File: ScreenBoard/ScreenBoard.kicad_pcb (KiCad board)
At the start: 4 copper layers, 37.5 x 35.6 mm, 21 parts, among them J3 Conn_01x09_Male, K1 K_0051, U1 U_0076

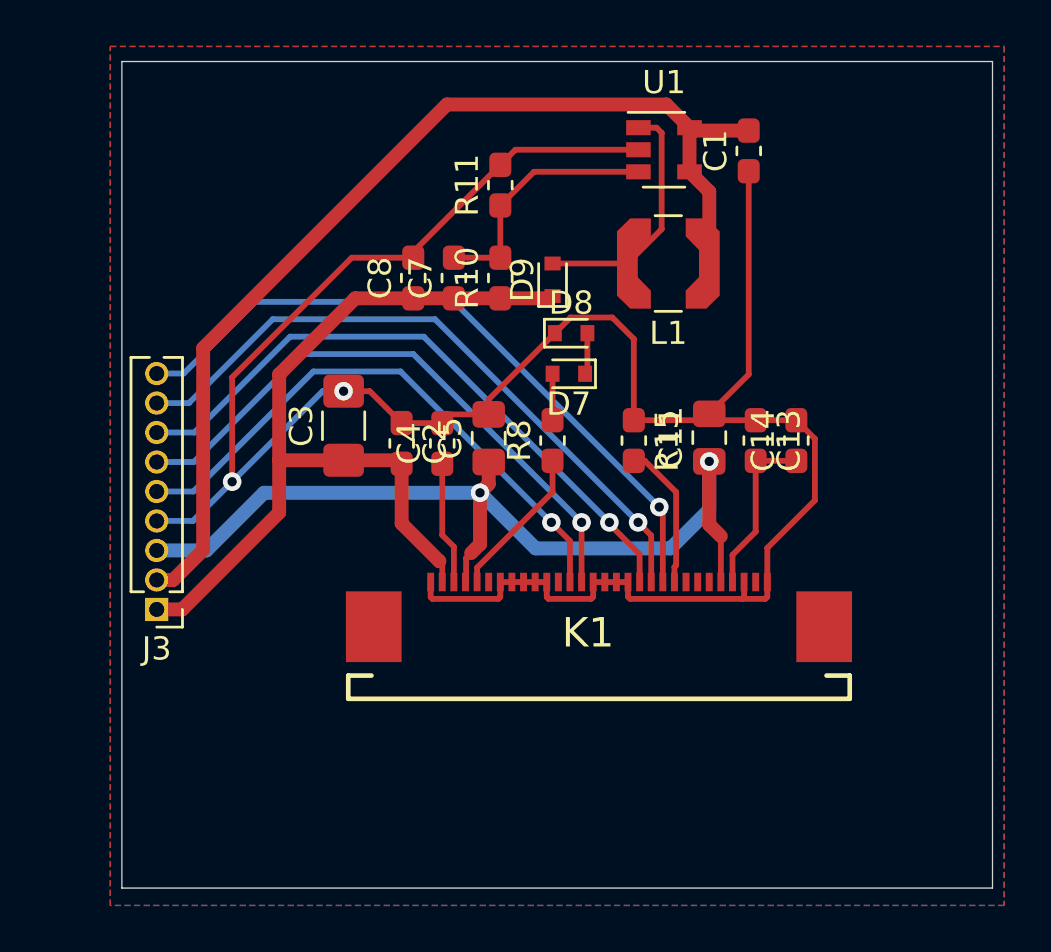
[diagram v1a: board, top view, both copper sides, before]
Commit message: fix: add missing rules and components
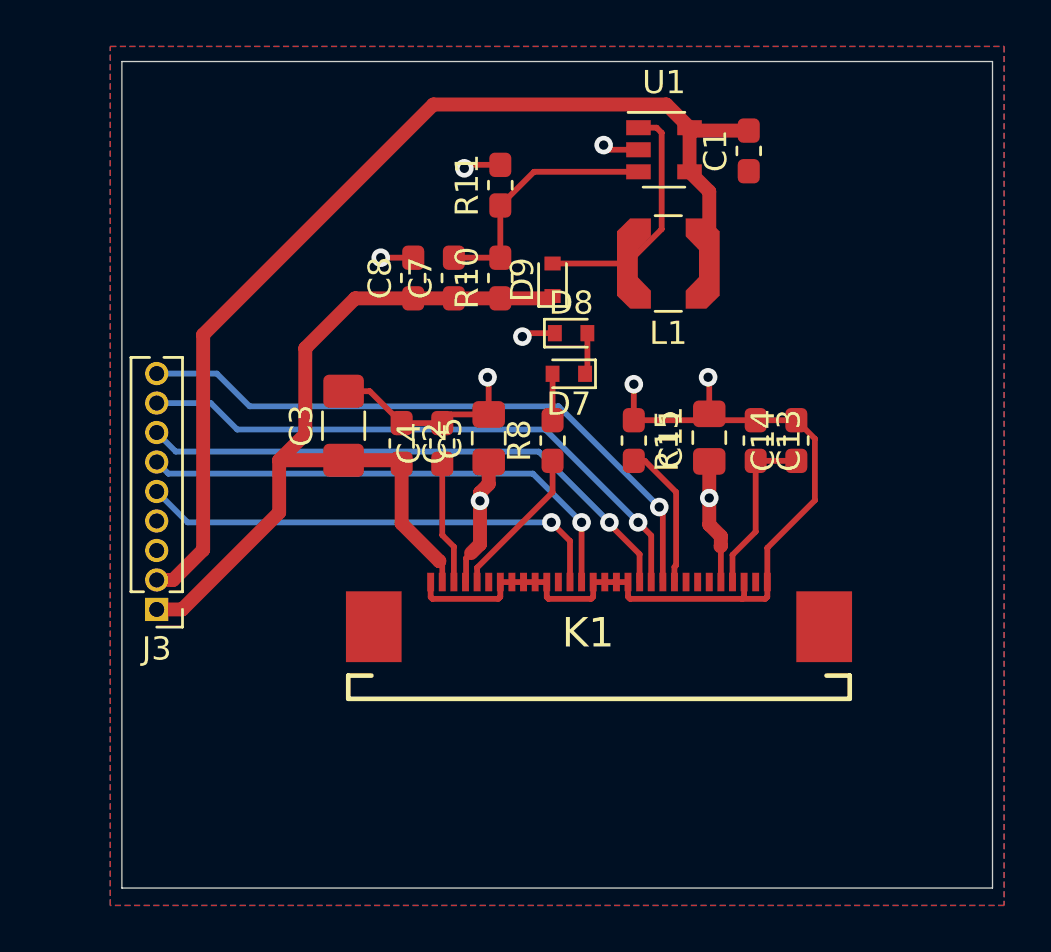
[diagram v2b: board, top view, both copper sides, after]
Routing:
- net GND: track 101.6 -> 52.5 mm, vias 2 -> 7
- net +3V3: track 39.6 -> 11.4 mm
- net /SPI1_MOSI: track 24.7 -> 20.5 mm
- net /SPI1_SCK: track 25.8 -> 21.9 mm
- net /OLED_CS: track 27.6 -> 24.2 mm
- net /OLED_DC: track 28.7 -> 25.7 mm
- net /OLED_RST: track 29.9 -> 27.3 mm

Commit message: fix: change screen connector footprint and adjust its mechanical position
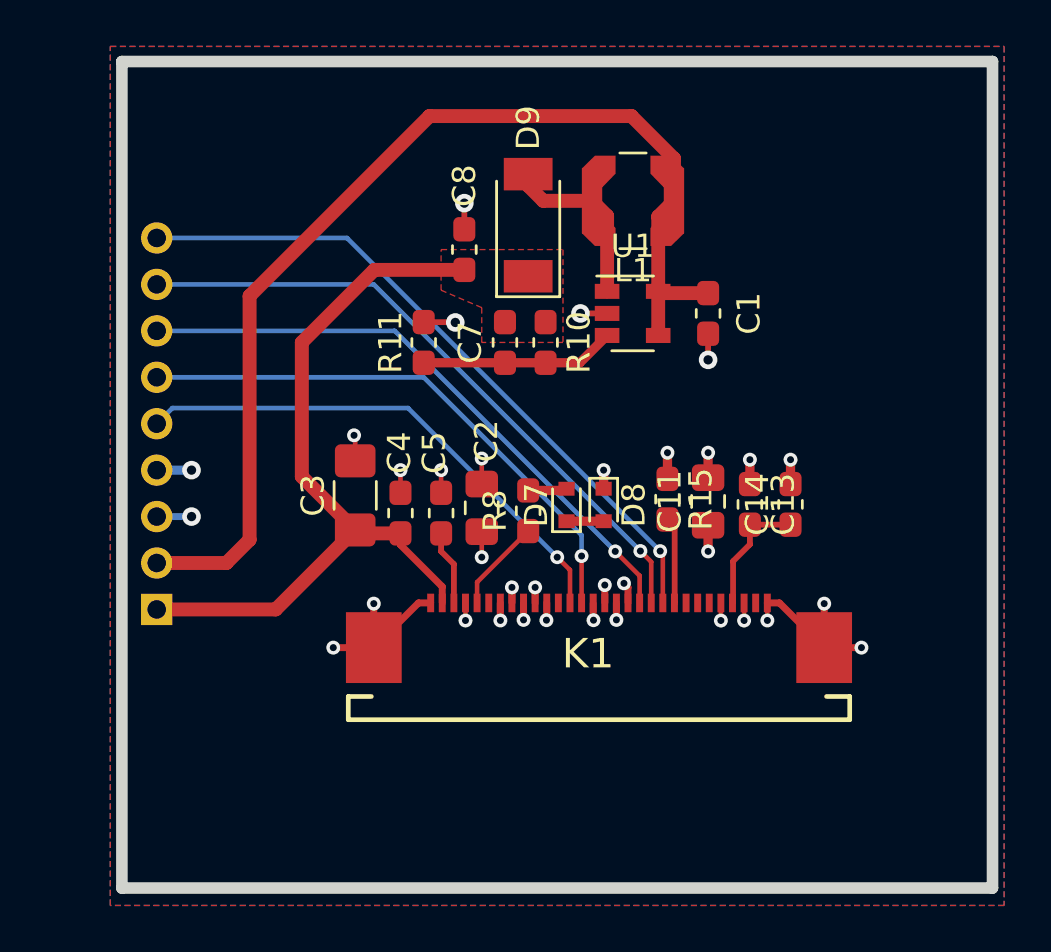
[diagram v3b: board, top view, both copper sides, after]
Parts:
- D9: footprint Diode_SMD:D_SOD-523 -> Diode_SMD:D_SOD-128
- J3: footprint Connector_PinHeader_1.27mm:PinHeader_1x09_P1.27mm_Vertical -> Connector_PinHeader_2.00mm:PinHeader_1x09_P2.00mm_Vertical; moved to B.Cu
- moved R11 7.54 mm to (114.0, 60.5)
- moved D8 7.53 mm to (121.8, 67.5), turned to 270 degrees
- moved C1 7.22 mm to (126.2, 59.2)
- moved U1 7.18 mm to (123.0, 59.2)
- moved D7 5.65 mm to (120.2, 67.5), turned to 90 degrees
- moved C7 3.54 mm to (117.5, 60.5), turned to 270 degrees
- moved R10 3.39 mm to (119.2, 60.5), turned to 270 degrees
- moved R8 3.20 mm to (118.5, 67.8)
- moved L1 3.10 mm to (123.0, 54.4)
- moved C3 3.04 mm to (111.0, 67.1)
- moved C5 3.01 mm to (116.5, 67.6)
- moved C2 3.00 mm to (113.0, 67.8)
- moved C4 3.00 mm to (114.8, 67.8)
- moved R15 2.91 mm to (124.5, 67.2)
- moved C13 2.76 mm to (128.1, 67.5)
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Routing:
- net GND: track 52.5 -> 38.9 mm, vias 7 -> 29
- net +12V: track 39.6 -> 33.0 mm
- net +3V3: track 11.4 -> 5.24 mm, vias 2 -> 5
- net Net-(D9-Pad2): track 10.6 -> 7.69 mm
- net Net-(K1-Pad5): track 6.57 -> 4.01 mm
- net Net-(K1-Pad22): track 6.28 -> 3.73 mm
- net Net-(C7-Pad2): track 10.8 -> 8.39 mm
- net /OLED_DC: track 25.7 -> 28.0 mm
- net /OLED_RST: track 27.3 -> 29.6 mm
- net /OLED_CS: track 24.2 -> 26.3 mm
- net /SPI1_SCK: track 21.9 -> 24.0 mm
- net Net-(C4-Pad1): track 5.30 -> 3.22 mm
- net Net-(C13-Pad2): track 7.38 -> 5.43 mm
- net /SPI1_MOSI: track 20.5 -> 22.4 mm
- net +5V: track 46.1 -> 47.2 mm
- added copper zone on F.Cu, net +12V

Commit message: adjust vias drill dimension to comply PCB provider rules
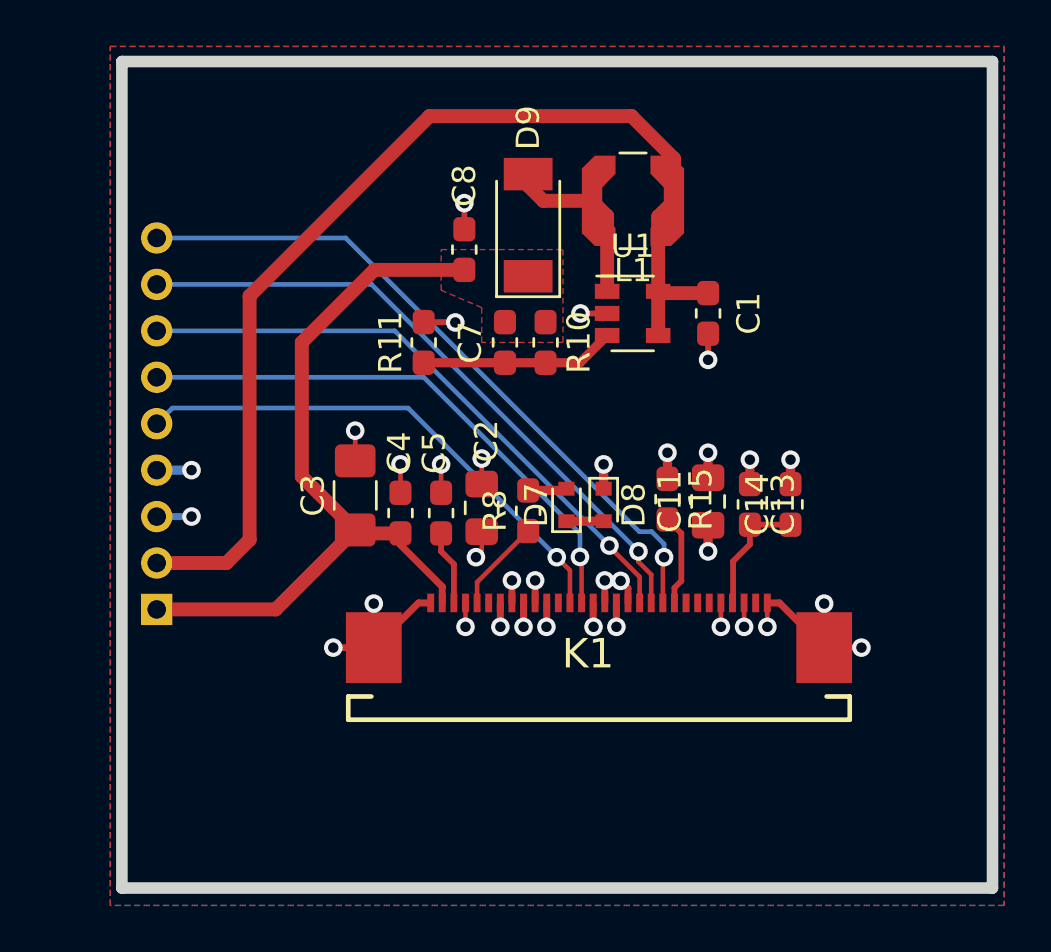
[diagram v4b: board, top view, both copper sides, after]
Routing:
- net GND: track 38.9 -> 42.8 mm
- net +3V3: track 5.24 -> 5.89 mm
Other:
- net class Default: via_drill 0.4 -> 0.45
- net class power: via_drill 0.4 -> 0.45

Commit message: fix and refactor: both mainboard and screenboard
Many improvements made
- Fixed all issues with footprints
- Optimized components placement and tracks
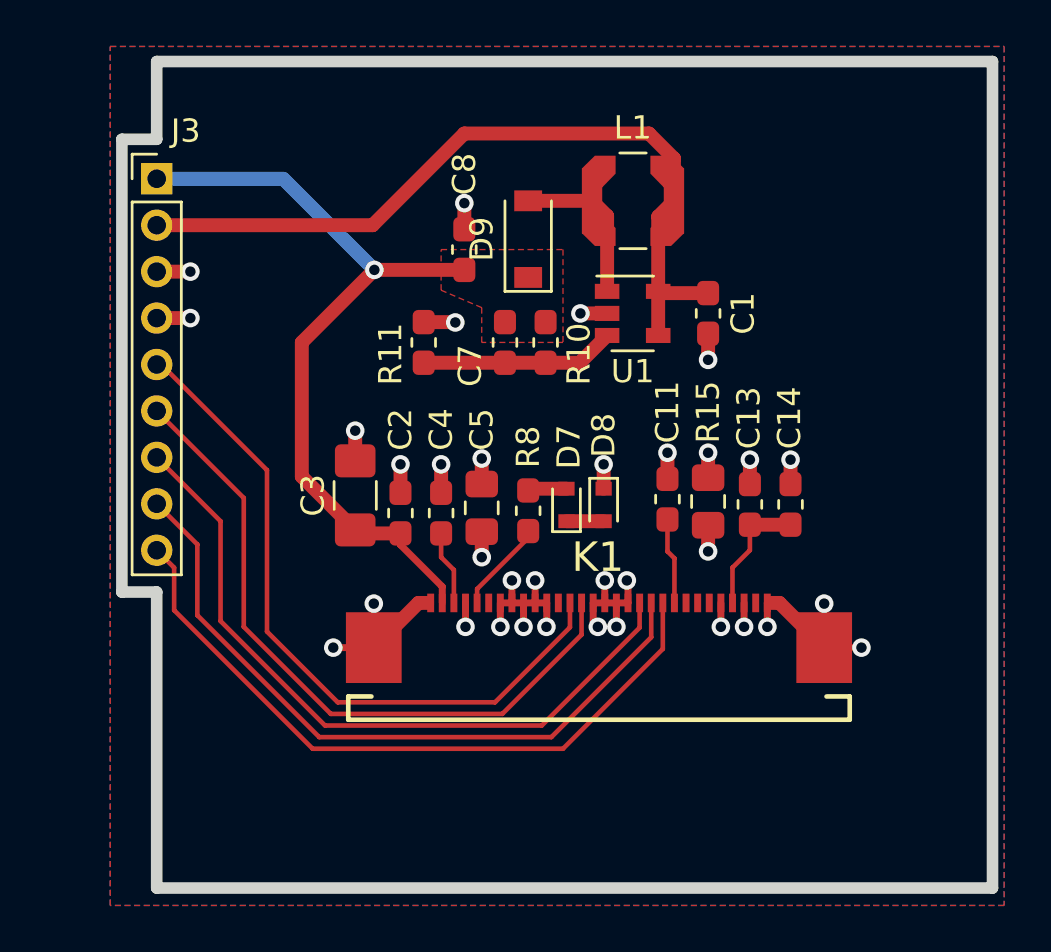
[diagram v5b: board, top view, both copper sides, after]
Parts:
- D9: footprint Diode_SMD:D_SOD-128 -> Diode_SMD:D_SOD-123
- J3: moved to F.Cu
- moved J3 18.5 mm to (102.5, 53.5)
- moved D9 0.60 mm to (118.5, 56.0)
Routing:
- net +5V: track 47.2 -> 34.4 mm
- net /SPI1_MOSI: track 22.4 -> 30.3 mm, vias 1 -> 0
- net /SPI1_SCK: track 24.0 -> 29.7 mm, vias 1 -> 0
- net /OLED_CS: track 26.3 -> 30.9 mm, vias 1 -> 0
- net /OLED_DC: track 28.0 -> 30.5 mm, vias 1 -> 0
- net GND: track 42.8 -> 44.6 mm
- net +12V: track 33.0 -> 34.1 mm, vias 0 -> 1
- net Net-(D9-Pad2): track 7.69 -> 6.92 mm
- net /OLED_RST: track 29.9 -> 30.2 mm, vias 1 -> 0
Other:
- outline, holes or cut-outs redrawn
- net class Default: trace_width 0.25 -> 0.2

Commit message: Finalized PCBs
- Add MicroSD Card support on screen board
- Fix Hall sensors footprints (flip board side)
- Change screen connector
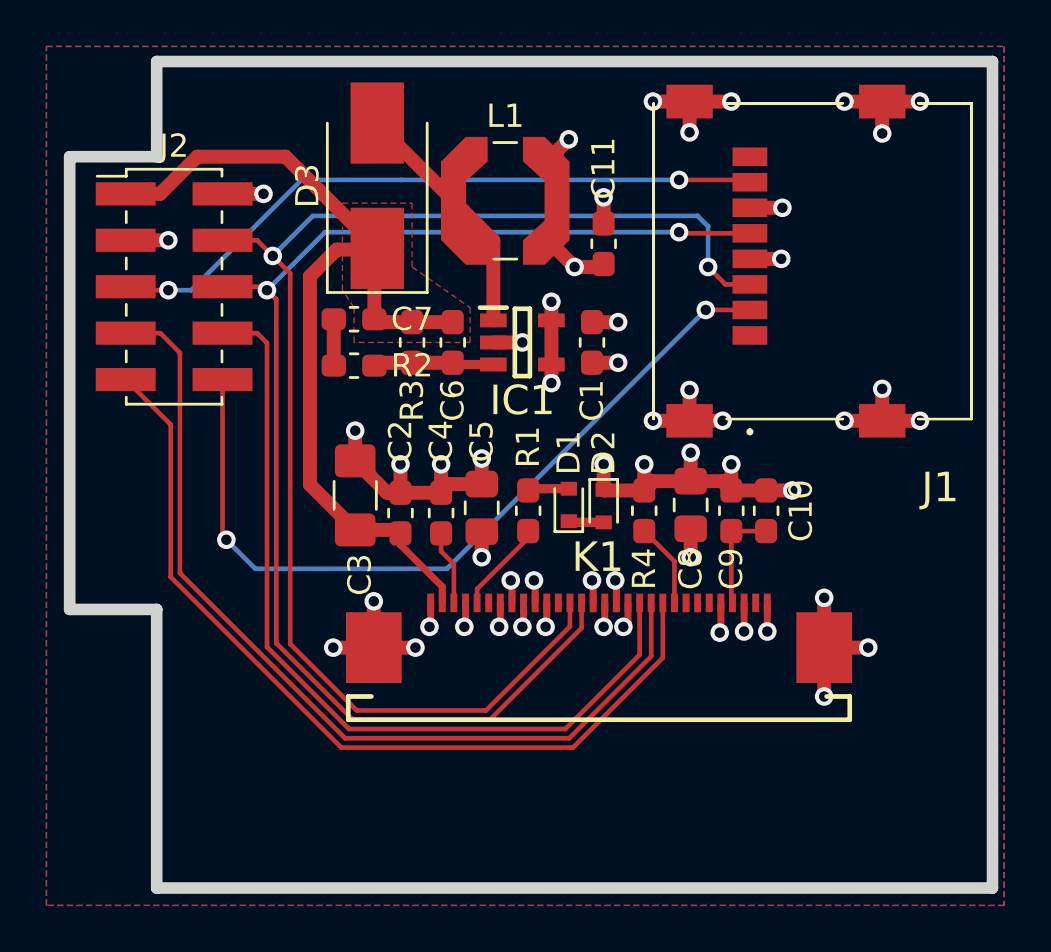
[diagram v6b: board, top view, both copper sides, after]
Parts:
- removed C13: C_0033, Capacitor_SMD:C_0603_1608Metric_Pad1.05x0.95mm_HandSolder
- removed C14: C_0036, Capacitor_SMD:C_0603_1608Metric_Pad1.05x0.95mm_HandSolder
- removed D7, D8: D_0022, Diode_SMD:D_SOD-523
- removed D9: D_0021, Diode_SMD:D_SOD-123
- removed J3: Conn_01x09_Male, Connector_PinHeader_2.00mm:PinHeader_1x09_P2.00mm_Vertical
- removed R10: R_0107, Resistor_SMD:R_0603_1608Metric_Pad1.05x0.95mm_HandSolder
- removed R11: R_0108, Resistor_SMD:R_0603_1608Metric_Pad1.05x0.95mm_HandSolder
- removed R15: R_0019, Resistor_SMD:R_0603_1608Metric_Pad1.05x0.95mm_HandSolder
- removed R8: R_0110, Resistor_SMD:R_0603_1608Metric_Pad1.05x0.95mm_HandSolder
- removed U1: U_0076, Package_TO_SOT_SMD:SOT-23-5
- added C10: 4.7µF, Capacitor_SMD:C_0603_1608Metric_Pad1.05x0.95mm_HandSolder, F.Cu at (128.8, 67.8)
- added C6: 120pF, Capacitor_SMD:C_0603_1608Metric_Pad1.05x0.95mm_HandSolder, F.Cu at (115.2, 60.5)
- added C9: 100nF, Capacitor_SMD:C_0603_1608Metric_Pad1.05x0.95mm_HandSolder, F.Cu at (127.2, 67.8)
- added D1: 1N4148WT, Diode_SMD:D_SOD-523, F.Cu at (120.2, 67.5)
- added D2: 1N4148WT, Diode_SMD:D_SOD-523, F.Cu at (121.8, 67.5)
- added D3: MBRS130LT3G, Diode_SMD:D_SMB_Handsoldering, F.Cu at (112.0, 53.8)
- added IC1: FAN5331SX, SamacSys_Parts:SOT95P280X145-5N, F.Cu at (118.2, 60.5)
- added J1: Micro_SD_Card, SamacSys_Parts:693072010801, F.Cu at (130.8, 57.0)
- added J2: Conn_02x05_Male, Connector_PinHeader_2.00mm:PinHeader_2x05_P2.00mm_Vertical_SMD, F.Cu at (103.2, 58.1)
- added R1: 56 Ohm, Resistor_SMD:R_0603_1608Metric_Pad1.05x0.95mm_HandSolder, F.Cu at (118.5, 67.8)
- added R2: 10k, Resistor_SMD:R_0603_1608Metric_Pad1.05x0.95mm_HandSolder, F.Cu at (111.0, 61.5)
- added R3: 100k, Resistor_SMD:R_0603_1608Metric_Pad1.05x0.95mm_HandSolder, F.Cu at (113.5, 60.5)
- added R4: 600k, Resistor_SMD:R_0603_1608Metric_Pad1.05x0.95mm_HandSolder, F.Cu at (123.5, 67.8)
- C1: value C_0003 -> 4.7µF
- C11: value C_0056 -> 10µF; footprint Capacitor_SMD:C_0805_2012Metric_Pad1.15x1.40mm_HandSolder -> Capacitor_SMD:C_0603_1608Metric_Pad1.05x0.95mm_HandSolder
- C2: value C_0033 -> 100nF
- C3: value C_0041 -> 10µF
- C4: value C_0036 -> 4.7µF
- C5: value C_0056 -> 1µF
- C7: value C_0013 -> 4.7µF
- C8: value C_0036 -> 1µF; footprint Capacitor_SMD:C_0603_1608Metric_Pad1.05x0.95mm_HandSolder -> Capacitor_SMD:C_0805_2012Metric_Pad1.15x1.40mm_HandSolder
- K1: value K_0051 -> OLED connector
- L1: value L_0011 -> 10µH; footprint Inductor_SMD:L_Coilcraft_LPS4018 -> Inductor_SMD:L_Coilcraft_LPS5030
- moved C8 14.7 mm to (125.5, 67.5)
- moved C11 12.0 mm to (121.8, 56.2), turned to 270 degrees
- moved C7 6.58 mm to (111.0, 59.5), turned to 0 degrees
- moved L1 5.50 mm to (117.5, 54.4)
- moved C1 5.15 mm to (121.2, 60.5)
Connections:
- C1 pad 2: +5V -> +3V3
- C11 pad 1: +3V3 -> GND
- C11 pad 2: GND -> +3V3
- C7 pad 1: +12V -> GND
- C7 pad 2: Net-(C7-Pad2) -> +12V
- C8 pad 1: +12V -> +3V3
- K1 pad 13: /SPI1_MOSI -> /SPI_MOSI
- K1 pad 14: /SPI1_SCK -> /SPI_SCK
- L1 pad 1: +5V -> +3V3
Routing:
- net /SPI_MOSI: track 0.00 -> 58.7 mm, vias 0 -> 2
- net /SPI_SCK: track 0.00 -> 56.4 mm, vias 0 -> 2
- net /SD_CS: track 0.00 -> 34.7 mm, vias 0 -> 2
- net +5V: track 34.4 -> 0.00 mm
- net GND: track 44.6 -> 75.5 mm, vias 29 -> 44
- net /SPI1_MOSI: track 30.3 -> 0.00 mm
- net /SPI1_SCK: track 29.7 -> 0.00 mm
- net /SPI_MISO: track 0.00 -> 29.0 mm, vias 0 -> 2
- net +3V3: track 5.73 -> 19.7 mm, vias 5 -> 11
- net /OLED_DC: track 30.5 -> 39.2 mm
- net Net-(C7-Pad2): track 8.39 -> 0.00 mm
- net /OLED_RST: track 30.2 -> 37.5 mm
- net +12V: track 34.1 -> 40.5 mm, vias 1 -> 0
- net /OLED_CS: track 30.9 -> 36.3 mm
- net Net-(C6-Pad1): track 0.00 -> 5.28 mm
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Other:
- board size 37.5 x 35.6 mm -> 39.8 x 35.6 mm
